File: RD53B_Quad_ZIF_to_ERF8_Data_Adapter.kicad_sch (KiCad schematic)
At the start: 7 parts, among them J2 Conn_02x01, J3 Conn_02x02_Odd_Even, J4 Conn_02x04_Odd_Even, J5 ERF8-050-01-X-D-EM2-TR, J6 Conn_02x01

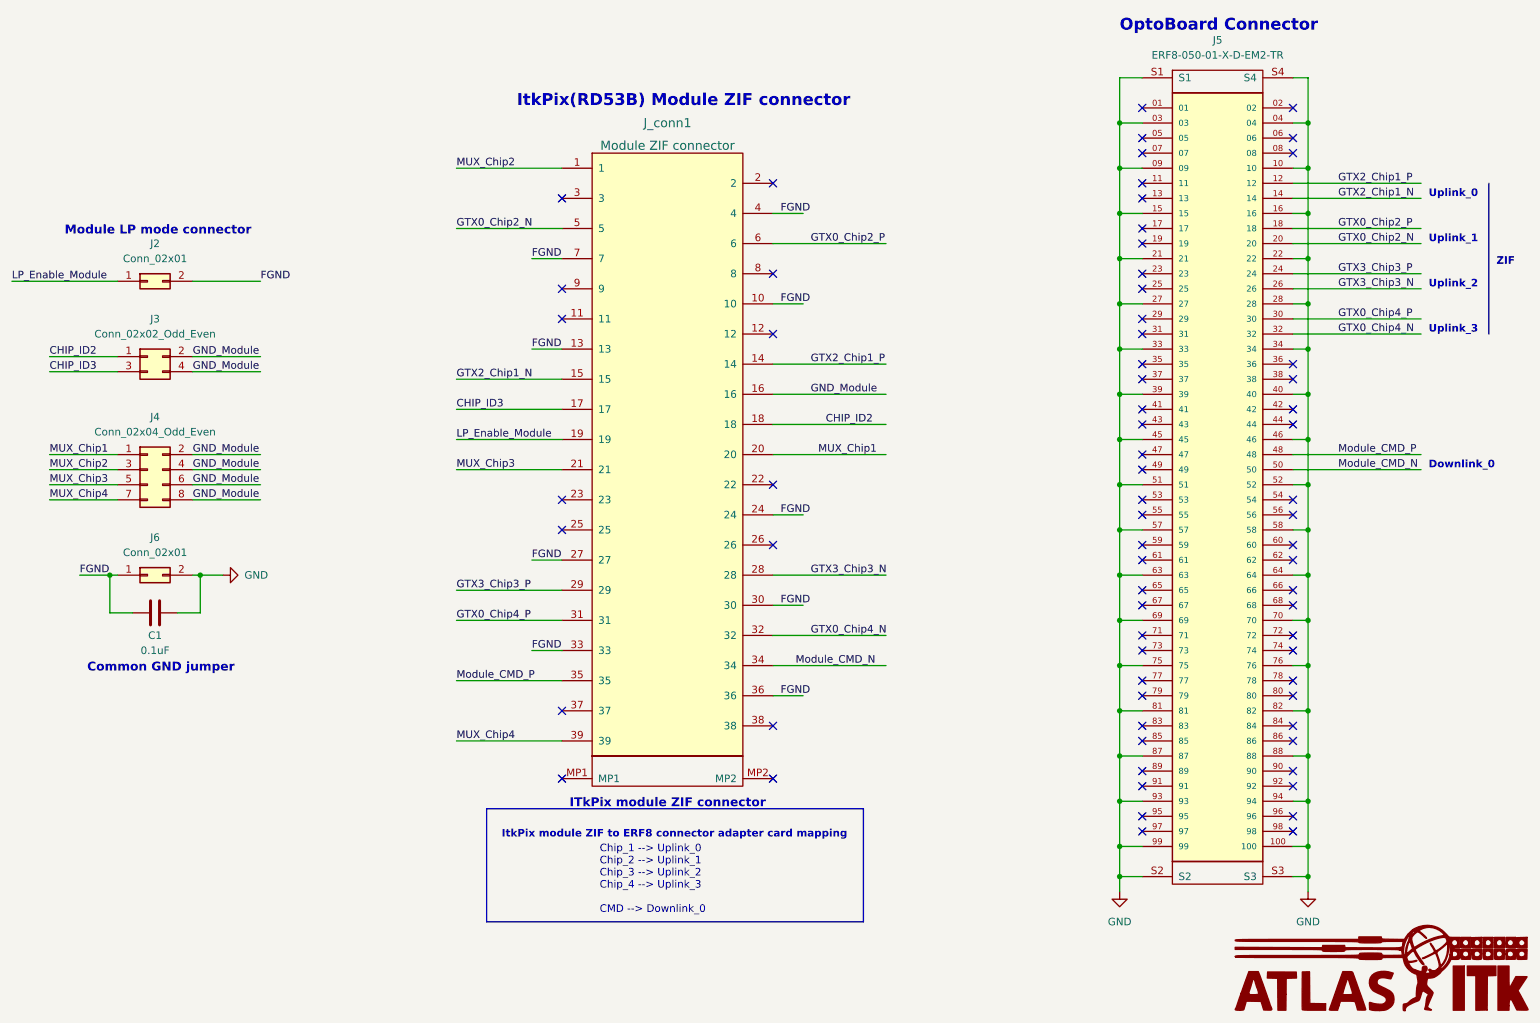
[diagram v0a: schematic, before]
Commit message: Change mapping to master LpGBT
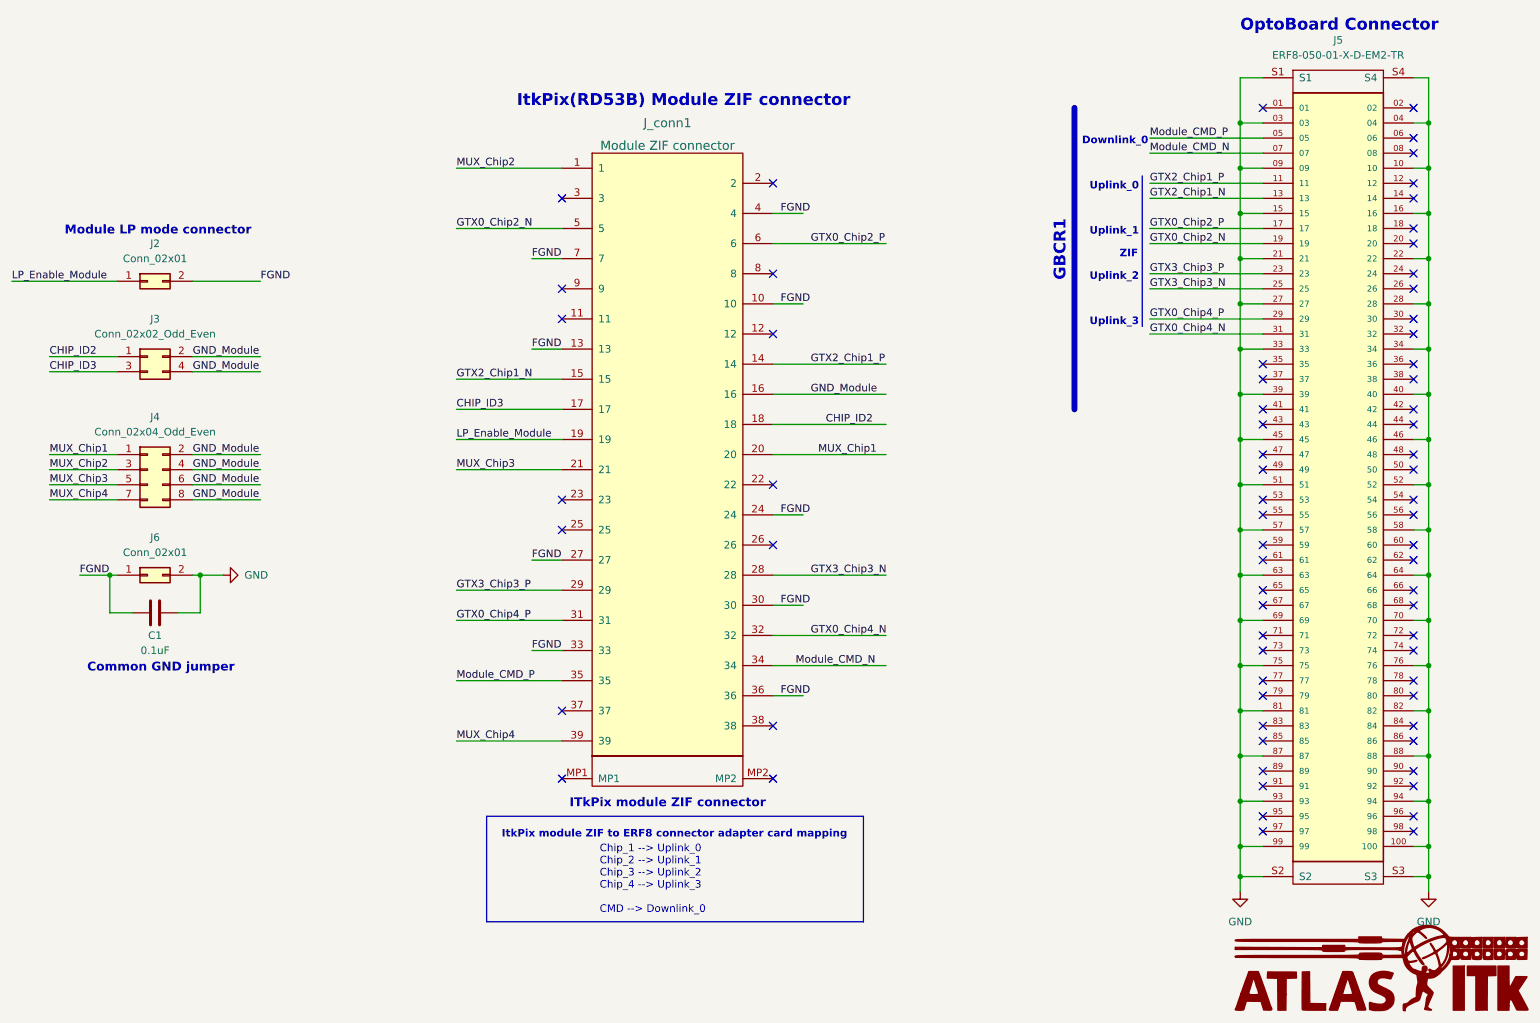
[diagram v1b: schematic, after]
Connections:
- net GTX0_Chip2_N: now also J5.19; no longer J5.20
- net GTX0_Chip2_P: now also J5.17; no longer J5.18
- net GTX0_Chip4_N: now also J5.31; no longer J5.32
- net GTX0_Chip4_P: now also J5.29; no longer J5.30
- net GTX2_Chip1_N: now also J5.13; no longer J5.14
- net GTX2_Chip1_P: now also J5.11; no longer J5.12
- net GTX3_Chip3_N: now also J5.25; no longer J5.26
- net GTX3_Chip3_P: now also J5.23; no longer J5.24
- net Module_CMD_N: now also J5.07; no longer J5.50
- net Module_CMD_P: now also J5.05; no longer J5.48
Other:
- note added: "GBCR1"
- moved on the sheet: J5

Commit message: update
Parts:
- renumbered J_conn1 to J1
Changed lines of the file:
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@@
     (stroke (width 0) (type default))
   )
-  (polyline (pts (xy 203.2 27.94) (xy 203.2 78.74))
+  (polyline (pts (xy 203.2 27.94) (xy 203.2 82.55))
     (stroke (width 1) (type default))
   )
@@
   (symbol (lib_id "Molex-502598-3993:ConnSingle") (at 132.08 93.98 0) (unit 1)
     (in_bom yes) (on_board yes) (dnp no) (fields_autoplaced)
-    (property "Reference" "J_conn1" (at 134.62 30.48 0)
+    (property "Reference" "J1" (at 134.62 30.48 0)
       (effects (font (size 1.524 1.524)))
     )
@@
       (project "RD53B_Quad_ZIF_to_ERF8_Data_Adapter"
         (path "/944dddd9-6642-49a0-962d-82b52e26316b"
-          (reference "J_conn1") (unit 1)
+          (reference "J1") (unit 1)
         )
       )
